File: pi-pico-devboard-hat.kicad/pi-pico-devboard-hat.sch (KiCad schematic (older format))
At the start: 20 parts, among them J1 Conn_01x24_Male, J2 I2C, J3 SDA_UP, J4 SCL_UP, J5 Conn_SPI, J6 Conn_Ext, J7 Conn_BTN, P1 Conn_02x20_Odd_Even, SW1 SW_Reset, SW2 BTN1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

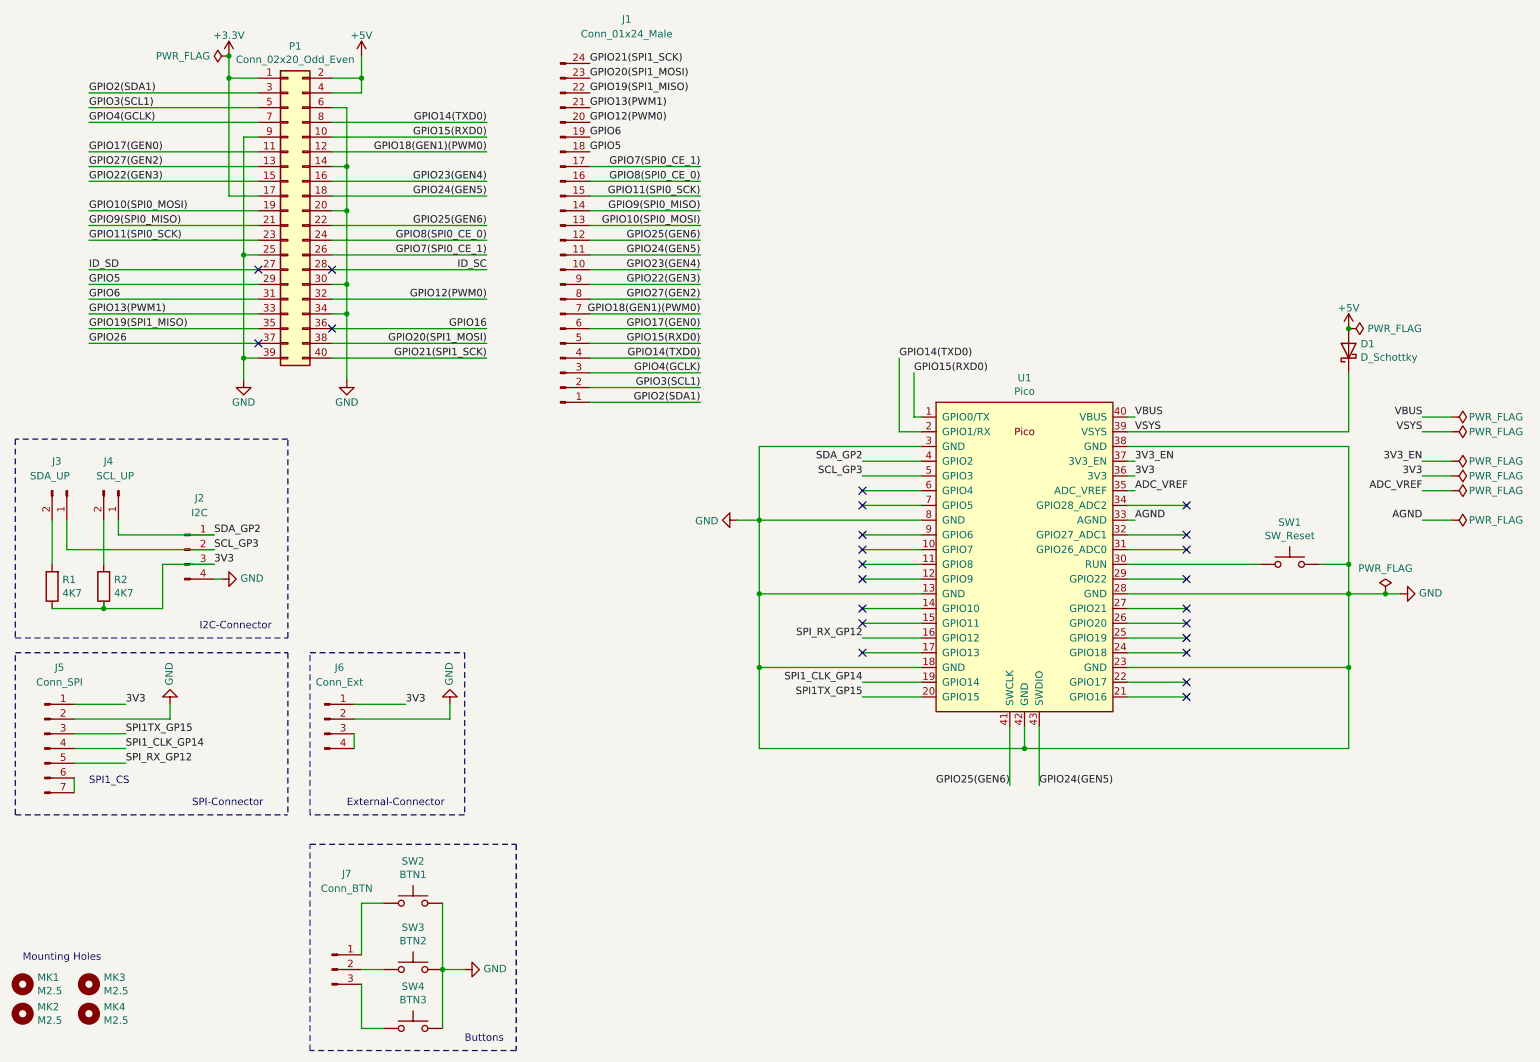
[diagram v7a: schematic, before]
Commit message: Rev 7: added LEDs
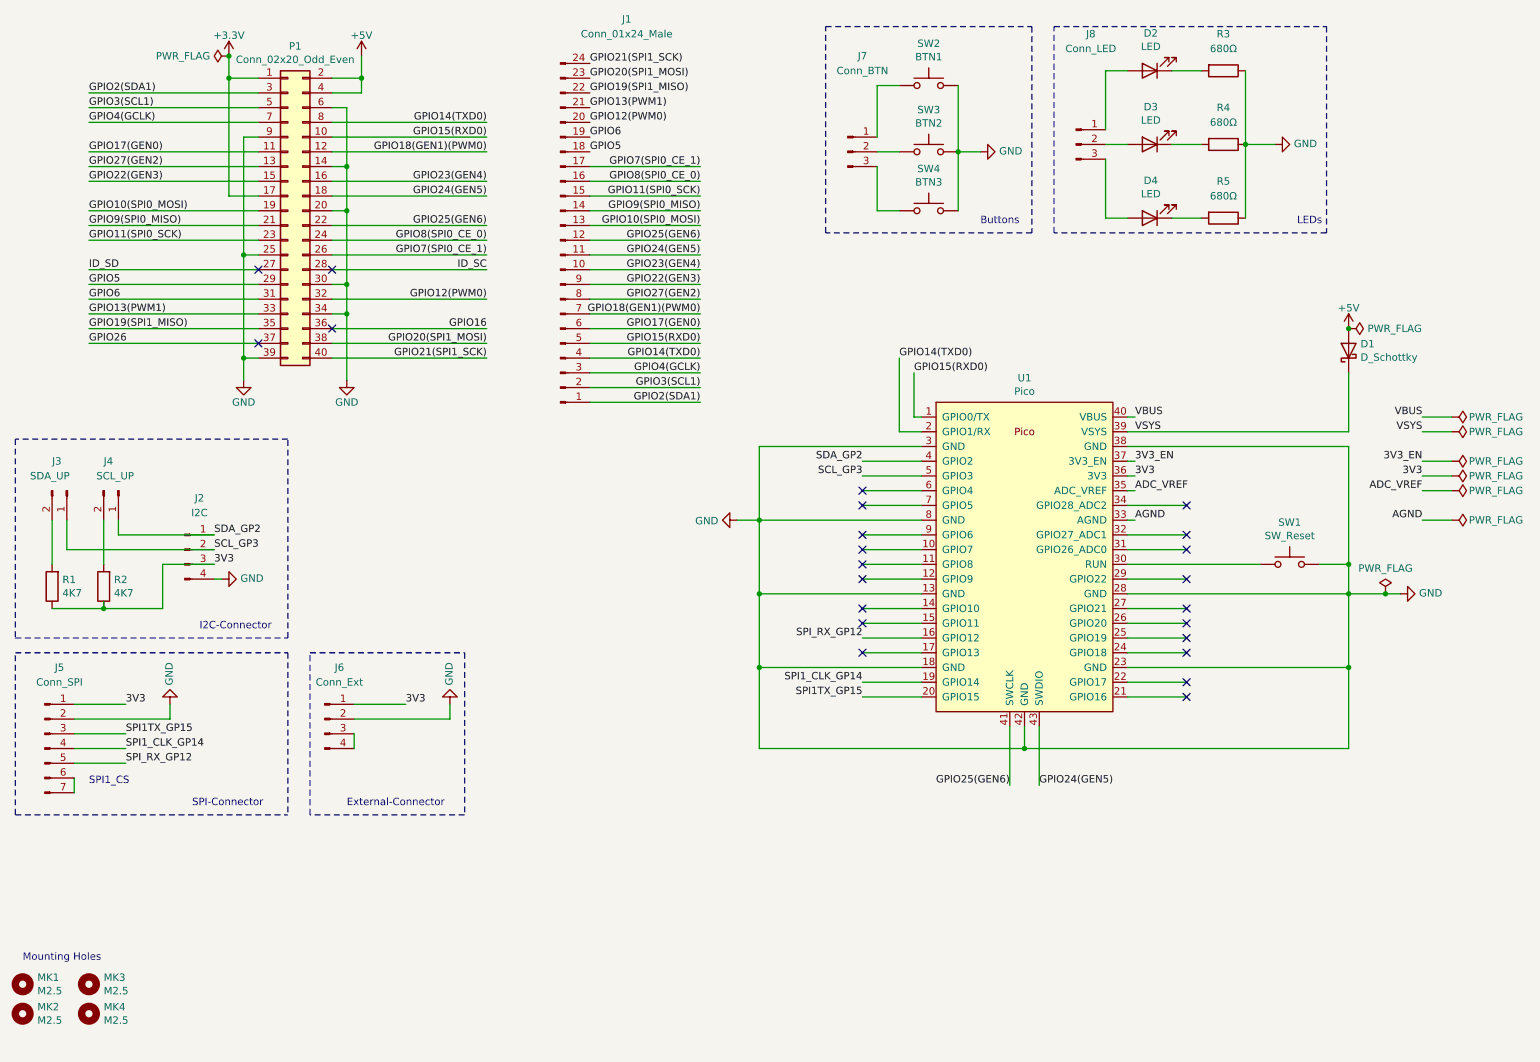
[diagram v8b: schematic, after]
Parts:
- added D2, D3, D4: LED, LED_THT:LED_D3.0mm, symbol Device:LED
- added J8: Conn_LED, Connector_PinHeader_2.54mm:PinHeader_1x03_P2.54mm_Vertical, symbol Connector:Conn_01x03_Male
- added R3, R4, R5: 680Ω, Resistor_THT:R_Axial_DIN0204_L3.6mm_D1.6mm_P5.08mm_Horizontal, symbol Device:R
- R1, R2: footprint Resistor_THT:R_Axial_DIN0207_L6.3mm_D2.5mm_P7.62mm_Horizontal -> Resistor_THT:R_Axial_DIN0204_L3.6mm_D1.6mm_P5.08mm_Horizontal
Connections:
- net GND: now also R3.1, R4.1, R5.1
- new net: D2.1 (K), R3.2
- new net: D2.2 (A), J8.1 (Pin_1)
- new net: D3.1 (K), R4.2
- new net: D3.2 (A), J8.2 (Pin_2)
- new net: D4.1 (K), R5.2
- new net: D4.2 (A), J8.3 (Pin_3)
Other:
- note added: "LEDs"
- moved on the sheet: J7, SW2, SW3, SW4
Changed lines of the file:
@@
 Title "pi-pico-devboard-hat"
 Date "2021-03-23"
-Rev "6"
+Rev "7"
 Comp "Bernhard Bablok"
 Comment1 "https://github.com/bablokb/pi-pico-devboard-hat"
@@
 F 0 "R2" H 1280 4504 50  0000 R CNN
 F 1 "4K7" H 1280 4595 50  0000 R CNN
-F 2 "Resistor_THT:R_Axial_DIN0207_L6.3mm_D2.5mm_P7.62mm_Horizontal" V 1280 4550 50  0001 C CNN
+F 2 "Resistor_THT:R_Axial_DIN0204_L3.6mm_D1.6mm_P5.08mm_Horizontal" V 1280 4550 50  0001 C CNN
 F 3 "~" H 1350 4550 50  0001 C CNN
 	1    1350 4550
@@
 F 0 "R1" H 930 4504 50  0000 R CNN
 F 1 "4K7" H 930 4595 50  0000 R CNN
-F 2 "Resistor_THT:R_Axial_DIN0207_L6.3mm_D2.5mm_P7.62mm_Horizontal" V 930 4550 50  0001 C CNN
+F 2 "Resistor_THT:R_Axial_DIN0204_L3.6mm_D1.6mm_P5.08mm_Horizontal" V 930 4550 50  0001 C CNN
 F 3 "~" H 1000 4550 50  0001 C CNN
 	1    1000 4550
@@
 L Switch:SW_Push SW2
 U 1 1 605E1ED2
-P 3450 6700
-F 0 "SW2" H 3450 6985 50  0000 C CNN
-F 1 "BTN1" H 3450 6894 50  0000 C CNN
-F 2 "user:SW_PUSH_SLIM_1x4" H 3450 6900 50  0001 C CNN
-F 3 "~" H 3450 6900 50  0001 C CNN
-	1    3450 6700
+P 6950 1150
+F 0 "SW2" H 6950 1435 50  0000 C CNN
+F 1 "BTN1" H 6950 1344 50  0000 C CNN
+F 2 "user:SW_PUSH_SLIM_1x4" H 6950 1350 50  0001 C CNN
+F 3 "~" H 6950 1350 50  0001 C CNN
+	1    6950 1150
 	1    0    0    -1
 $EndComp
@@
 L Switch:SW_Push SW3
 U 1 1 605EB865
-P 3450 7150
-F 0 "SW3" H 3450 7435 50  0000 C CNN
-F 1 "BTN2" H 3450 7344 50  0000 C CNN
-F 2 "user:SW_PUSH_SLIM_1x4" H 3450 7350 50  0001 C CNN
-F 3 "~" H 3450 7350 50  0001 C CNN
-	1    3450 7150
+P 6950 1600
+F 0 "SW3" H 6950 1885 50  0000 C CNN
+F 1 "BTN2" H 6950 1794 50  0000 C CNN
+F 2 "user:SW_PUSH_SLIM_1x4" H 6950 1800 50  0001 C CNN
+F 3 "~" H 6950 1800 50  0001 C CNN
+	1    6950 1600
 	1    0    0    -1
 $EndComp
@@
 L Switch:SW_Push SW4
 U 1 1 605EBC25
-P 3450 7550
-F 0 "SW4" H 3450 7835 50  0000 C CNN
-F 1 "BTN3" H 3450 7744 50  0000 C CNN
-F 2 "user:SW_PUSH_SLIM_1x4" H 3450 7750 50  0001 C CNN
-F 3 "~" H 3450 7750 50  0001 C CNN
-	1    3450 7550
+P 6950 2000
+F 0 "SW4" H 6950 2285 50  0000 C CNN
+F 1 "BTN3" H 6950 2194 50  0000 C CNN
+F 2 "user:SW_PUSH_SLIM_1x4" H 6950 2200 50  0001 C CNN
+F 3 "~" H 6950 2200 50  0001 C CNN
+	1    6950 2000
 	1    0    0    -1
 $EndComp
@@
 L Connector:Conn_01x03_Male J7
 U 1 1 605EC64E
-P 2900 7150
-F 0 "J7" H 3000 7800 50  0000 C CNN
-F 1 "Conn_BTN" H 3000 7700 50  0000 C CNN
-F 2 "Connector_PinHeader_2.54mm:PinHeader_1x03_P2.54mm_Vertical" H 2900 7150 50  0001 C CNN
-F 3 "~" H 2900 7150 50  0001 C CNN
-	1    2900 7150
+P 6400 1600
+F 0 "J7" H 6500 2250 50  0000 C CNN
+F 1 "Conn_BTN" H 6500 2150 50  0000 C CNN
+F 2 "Connector_PinHeader_2.54mm:PinHeader_1x03_P2.54mm_Vertical" H 6400 1600 50  0001 C CNN
+F 3 "~" H 6400 1600 50  0001 C CNN
+	1    6400 1600
 	1    0    0    -1
 $EndComp
@@
 L power:GND #PWR09
 U 1 1 605ED18C
-P 3800 7150
-F 0 "#PWR09" H 3800 6900 50  0001 C CNN
-F 1 "GND" V 3805 7022 50  0000 R CNN
-F 2 "" H 3800 7150 50  0001 C CNN
-F 3 "" H 3800 7150 50  0001 C CNN
-	1    3800 7150
+P 7300 1600
+F 0 "#PWR09" H 7300 1350 50  0001 C CNN
+F 1 "GND" V 7305 1472 50  0000 R CNN
+F 2 "" H 7300 1600 50  0001 C CNN
+F 3 "" H 7300 1600 50  0001 C CNN
+	1    7300 1600
 	0    -1   -1   0
 $EndComp
 Wire Wire Line
-	3650 6700 3650 7150
-Connection ~ 3650 7150
-Wire Wire Line
-	3650 7150 3650 7550
-Wire Wire Line
-	3100 7050 3100 6700
-Wire Wire Line
-	3100 7250 3100 7550
-Wire Wire Line
-	3100 6700 3250 6700
-Wire Wire Line
-	3100 7150 3250 7150
-Wire Wire Line
-	3100 7550 3250 7550
-Wire Wire Line
-	3650 7150 3800 7150
-Wire Notes Line
-	2750 6300 4150 6300
-Wire Notes Line
-	4150 6300 4150 7700
-Wire Notes Line
-	4150 7700 2750 7700
-Wire Notes Line
-	2750 7700 2750 6300
-Text Notes 3800 7650 0    50   ~ 0
+	7150 1150 7150 1600
+Connection ~ 7150 1600
+Wire Wire Line
+	7150 1600 7150 2000
+Wire Wire Line
+	6600 1500 6600 1150
+Wire Wire Line
+	6600 1700 6600 2000
+Wire Wire Line
+	6600 1150 6750 1150
+Wire Wire Line
+	6600 1600 6750 1600
+Wire Wire Line
+	6600 2000 6750 2000
+Wire Wire Line
+	7150 1600 7300 1600
+Wire Notes Line
+	6250 750  7650 750
+Wire Notes Line
+	7650 750  7650 2150
+Wire Notes Line
+	7650 2150 6250 2150
+Wire Notes Line
+	6250 2150 6250 750
+Text Notes 7300 2100 0    50   ~ 0
 Buttons
+$Comp
+L Device:LED D2
+U 1 1 60698DA9
+P 8450 1050
+F 0 "D2" H 8443 795 50  0000 C CNN
+F 1 "LED" H 8443 886 50  0000 C CNN
+F 2 "LED_THT:LED_D3.0mm" H 8450 1050 50  0001 C CNN
+F 3 "~" H 8450 1050 50  0001 C CNN
+	1    8450 1050
+	-1   0    0    1
+$EndComp
+$Comp
+L Device:R R3
+U 1 1 60699DF2
+P 8950 1050
+F 0 "R3" V 8700 1050 50  0000 C CNN
+F 1 "680Ω" V 8800 1050 50  0000 C CNN
+F 2 "Resistor_THT:R_Axial_DIN0204_L3.6mm_D1.6mm_P5.08mm_Horizontal" V 8880 1050 50  0001 C CNN
+F 3 "~" H 8950 1050 50  0001 C CNN
+	1    8950 1050
+	0    1    1    0
+$EndComp
+$Comp
+L Device:LED D3
+U 1 1 6069B171
+P 8450 1550
+F 0 "D3" H 8443 1295 50  0000 C CNN
+F 1 "LED" H 8443 1386 50  0000 C CNN
+F 2 "LED_THT:LED_D3.0mm" H 8450 1550 50  0001 C CNN
+F 3 "~" H 8450 1550 50  0001 C CNN
+	1    8450 1550
+	-1   0    0    1
+$EndComp
+$Comp
+L Device:R R4
+U 1 1 6069B177
+P 8950 1550
+F 0 "R4" V 8700 1550 50  0000 C CNN
+F 1 "680Ω" V 8800 1550 50  0000 C CNN
+F 2 "Resistor_THT:R_Axial_DIN0204_L3.6mm_D1.6mm_P5.08mm_Horizontal" V 8880 1550 50  0001 C CNN
+F 3 "~" H 8950 1550 50  0001 C CNN
+	1    8950 1550
+	0    1    1    0
+$EndComp
+$Comp
+L Device:LED D4
+U 1 1 606A46FA
+P 8450 2050
+F 0 "D4" H 8443 1795 50  0000 C CNN
+F 1 "LED" H 8443 1886 50  0000 C CNN
+F 2 "LED_THT:LED_D3.0mm" H 8450 2050 50  0001 C CNN
+F 3 "~" H 8450 2050 50  0001 C CNN
+	1    8450 2050
+	-1   0    0    1
+$EndComp
+$Comp
+L Device:R R5
+U 1 1 606A4700
+P 8950 2050
+F 0 "R5" V 8700 2050 50  0000 C CNN
+F 1 "680Ω" V 8800 2050 50  0000 C CNN
+F 2 "Resistor_THT:R_Axial_DIN0204_L3.6mm_D1.6mm_P5.08mm_Horizontal" V 8880 2050 50  0001 C CNN
+F 3 "~" H 8950 2050 50  0001 C CNN
+	1    8950 2050
+	0    1    1    0
+$EndComp
+$Comp
+L power:GND #PWR010
+U 1 1 606B6298
+P 9300 1550
+F 0 "#PWR010" H 9300 1300 50  0001 C CNN
+F 1 "GND" V 9305 1422 50  0000 R CNN
+F 2 "" H 9300 1550 50  0001 C CNN
+F 3 "" H 9300 1550 50  0001 C CNN
+	1    9300 1550
+	0    -1   -1   0
+$EndComp
+$Comp
+L Connector:Conn_01x03_Male J8
+U 1 1 606B6B69
+P 7950 1550
+F 0 "J8" H 8050 2300 50  0000 C CNN
+F 1 "Conn_LED" H 8050 2200 50  0000 C CNN
+F 2 "Connector_PinHeader_2.54mm:PinHeader_1x03_P2.54mm_Vertical" H 7950 1550 50  0001 C CNN
+F 3 "~" H 7950 1550 50  0001 C CNN
+	1    7950 1550
+	1    0    0    -1
+$EndComp
+Wire Wire Line
+	9100 1050 9100 1550
+Wire Wire Line
+	9300 1550 9100 1550
+Connection ~ 9100 1550
+Wire Wire Line
+	9100 1550 9100 2050
+Wire Wire Line
+	8600 1050 8800 1050
+Wire Wire Line
+	8600 1550 8800 1550
+Wire Wire Line
+	8600 2050 8800 2050
+Wire Wire Line
+	8150 1450 8150 1050
+Wire Wire Line
+	8150 1050 8300 1050
+Wire Wire Line
+	8150 1550 8300 1550
+Wire Wire Line
+	8150 1650 8150 2050
+Wire Wire Line
+	8150 2050 8300 2050
+Wire Notes Line
+	7800 750  9650 750
+Wire Notes Line
+	9650 750  9650 2150
+Wire Notes Line
+	9650 2150 7800 2150
+Wire Notes Line
+	7800 2150 7800 750
+Text Notes 9450 2100 0    50   ~ 0
+LEDs
 $EndSCHEMATC
